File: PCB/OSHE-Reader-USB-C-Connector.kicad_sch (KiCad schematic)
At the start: 3 parts, among them J2 USB_C_Receptacle

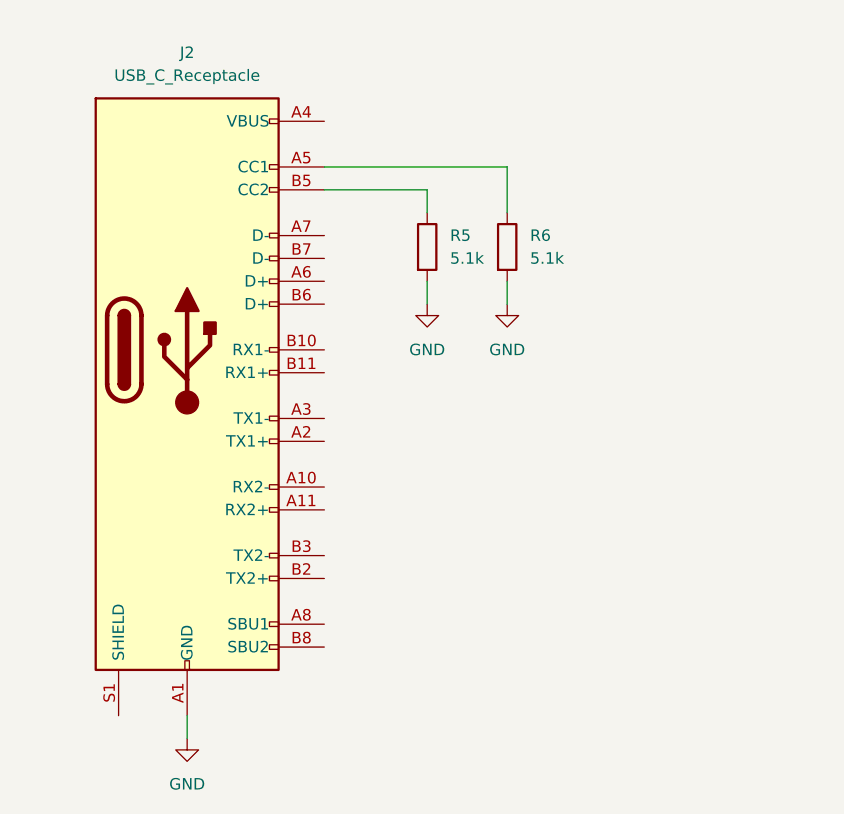
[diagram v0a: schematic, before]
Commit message: maybe finished usbc connector, depends on if we want to read CC lines for power adjustment
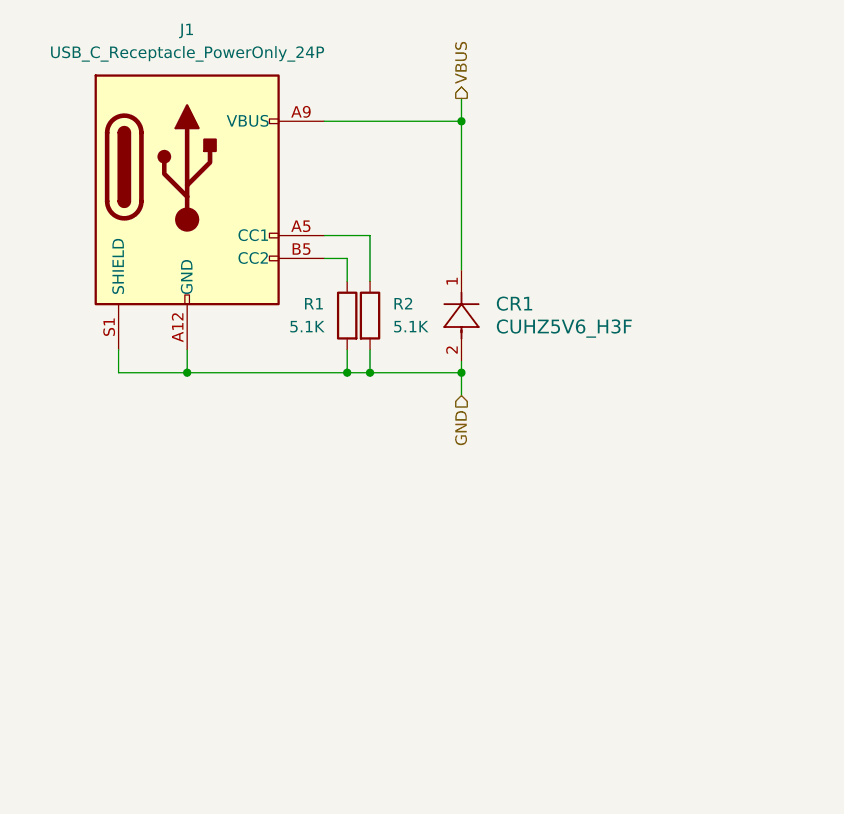
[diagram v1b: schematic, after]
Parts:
- removed J2: USB_C_Receptacle, symbol Connector:USB_C_Receptacle
- removed R5, R6: 5.1k, symbol Device:R
- added CR1: CUHZ5V6_H3F, SOD-323HEUS2H_TOS, symbol CUHZ5V6_H3F:CUHZ5V6_H3F
- added J1: USB_C_Receptacle_PowerOnly_24P, symbol Connector:USB_C_Receptacle_PowerOnly_24P
- added R1, R2: 5.1K, symbol Device:R
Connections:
- net GND: now also CR1.2, J1.A1 (GND), J1.A12 (GND), J1.B1 (GND), J1.B12 (GND), J1.S1 (SHIELD), R1.2, R2.2
- new net: J1.B5 (CC2), R1.1
- new net: J1.A5 (CC1), R2.1
- new net VBUS: CR1.1, J1.A4 (VBUS), J1.A9 (VBUS), J1.B4 (VBUS), J1.B9 (VBUS)

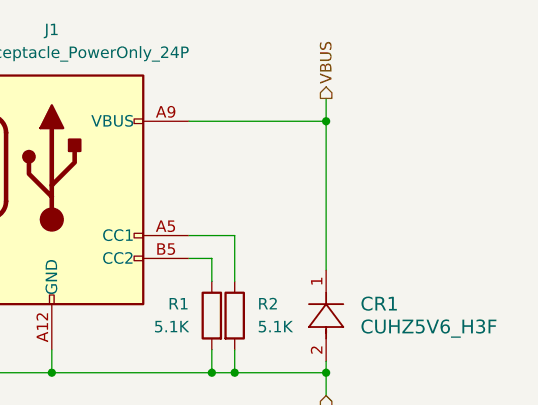
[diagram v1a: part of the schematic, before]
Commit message: fixed up the pcb so everything is *basically* passing ERC
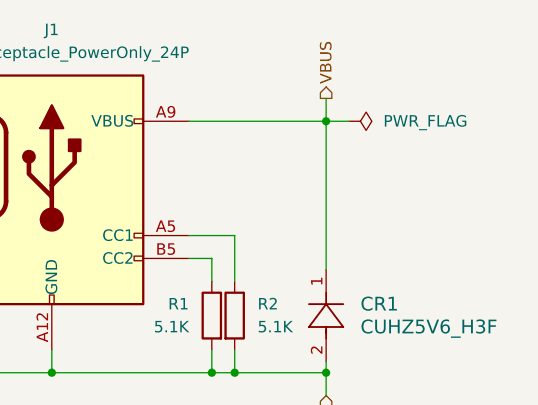
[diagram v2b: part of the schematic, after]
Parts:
- CR1: footprint SOD-323HEUS2H_TOS -> CUHZ5V6_H3F:SOD-323HEUS2H_TOS
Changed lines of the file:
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@@
+	(wire
+		(pts
+			(xy 68.58 33.02) (xy 71.12 33.02)
+		)
+		(stroke
+			(width 0)
+			(type default)
+		)
+	)
 	(wire
 		(pts
@@
 	)
 	(symbol
+		(lib_id "power:PWR_FLAG")
+		(at 71.12 33.02 270)
+		(unit 1)
+		(exclude_from_sim no)
+		(in_bom yes)
+		(on_board yes)
+		(dnp no)
+		(fields_autoplaced yes)
+		(property "Reference" "#FLG03"
+			(at 73.025 33.02 0)
+			(effects
+				(font
+					(size 1.27 1.27)
+				)
+				(hide yes)
+			)
+		)
+		(property "Value" "PWR_FLAG"
+			(at 74.93 33.0199 90)
+			(effects
+				(font
+					(size 1.27 1.27)
+				)
+				(justify left)
+			)
+		)
+		(property "Footprint" ""
+			(at 71.12 33.02 0)
+			(effects
+				(font
+					(size 1.27 1.27)
+				)
+				(hide yes)
+			)
+		)
+		(property "Datasheet" "~"
+			(at 71.12 33.02 0)
+			(effects
+				(font
+					(size 1.27 1.27)
+				)
+				(hide yes)
+			)
+		)
+		(property "Description" "Special symbol for telling ERC where power comes from"
+			(at 71.12 33.02 0)
+			(effects
+				(font
+					(size 1.27 1.27)
+				)
+				(hide yes)
+			)
+		)
+		(pin "1"
+		)
+		(instances
+			(project ""
+				(path "/3f072c92-e35a-4654-839b-728bd3dc3a46/026272d1-c63e-4075-9457-2aa47fc1f981"
+					(reference "#FLG03")
+					(unit 1)
+				)
+			)
+		)
+	)
+	(symbol
 		(lib_id "CUHZ5V6_H3F:CUHZ5V6_H3F")
 		(at 68.58 59.69 90)
@@
 			)
 		)
-		(property "Footprint" "SOD-323HEUS2H_TOS"
+		(property "Footprint" "CUHZ5V6_H3F:SOD-323HEUS2H_TOS"
 			(at 68.58 59.69 0)
 			(effects

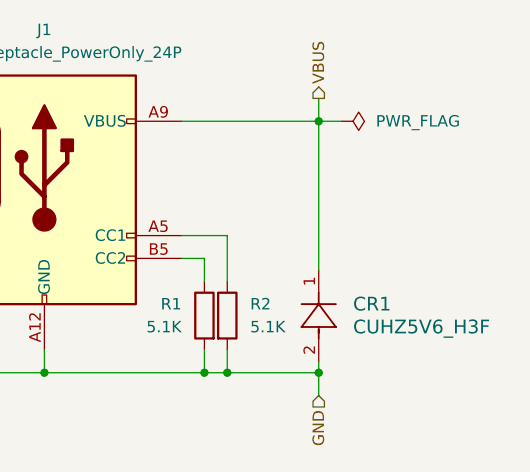
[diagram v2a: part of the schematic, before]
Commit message: work on pcb, adjusted components and started building ribbon connector for display
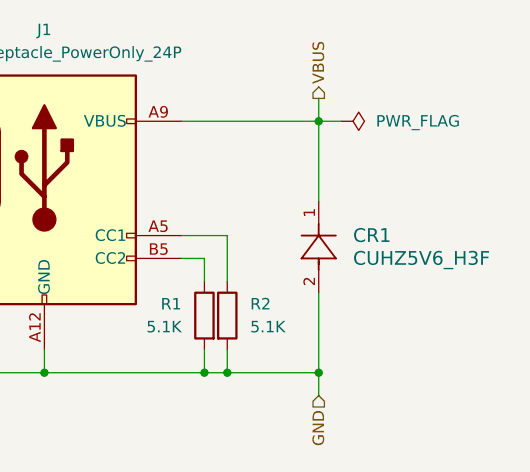
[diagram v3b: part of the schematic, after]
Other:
- moved on the sheet: CR1
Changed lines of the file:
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@@
 	(wire
 		(pts
-			(xy 68.58 60.96) (xy 68.58 59.69)
-		)
-		(stroke
-			(width 0)
-			(type default)
-		)
-	)
-	(wire
-		(pts
-			(xy 68.58 49.53) (xy 68.58 33.02)
+			(xy 68.58 60.96) (xy 68.58 52.07)
+		)
+		(stroke
+			(width 0)
+			(type default)
+		)
+	)
+	(wire
+		(pts
+			(xy 68.58 41.91) (xy 68.58 33.02)
 		)
 		(stroke
@@
 	(symbol
 		(lib_id "CUHZ5V6_H3F:CUHZ5V6_H3F")
-		(at 68.58 59.69 90)
+		(at 68.58 52.07 90)
 		(unit 1)
 		(exclude_from_sim no)
@@
 		(fields_autoplaced yes)
 		(property "Reference" "CR1"
-			(at 72.39 53.3399 90)
+			(at 72.39 45.7199 90)
 			(effects
 				(font
@@
 		)
 		(property "Value" "CUHZ5V6_H3F"
-			(at 72.39 55.8799 90)
+			(at 72.39 48.2599 90)
 			(effects
 				(font
@@
 		)
 		(property "Footprint" "CUHZ5V6_H3F:SOD-323HEUS2H_TOS"
-			(at 68.58 59.69 0)
+			(at 68.58 52.07 0)
 			(effects
 				(font
@@
 		)
 		(property "Datasheet" "https://toshiba.semicon-storage.com/info/docget.jsp?did=141580&prodName=CUHZ5V6"
-			(at 68.58 59.69 0)
+			(at 68.58 52.07 0)
 			(effects
 				(font
@@
 		)
 		(property "Description" ""
-			(at 68.58 59.69 0)
-			(effects
-				(font
+			(at 68.58 52.07 0)
+			(effects
+				(font

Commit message: added usbc connector symbol, footprint, and model, updated symbol in schematic
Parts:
- J1: footprint (none) -> USB4125_GF_A:CONN6_USB4125_GCT
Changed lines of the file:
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@@
 			)
 		)
-		(property "Footprint" ""
+		(property "Footprint" "USB4125_GF_A:CONN6_USB4125_GCT"
 			(at 41.91 38.1 0)
 			(effects

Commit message: HOPEFULLY GOOD FOR EVER (good for first semester) :)
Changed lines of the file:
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@@
-	(wire
-		(pts
-			(xy 68.58 33.02) (xy 71.12 33.02)
-		)
-		(stroke
-			(width 0)
-			(type default)
-		)
-	)
 	(wire
 		(pts
@@
 	)
 	(hierarchical_label "GND"
-		(shape input)
+		(shape output)
 		(at 68.58 63.5 270)
 		(effects
@@
 					(unit 1)
 				)
-			)
-		)
-	)
-	(symbol
-		(lib_id "power:PWR_FLAG")
-		(at 71.12 33.02 270)
-		(unit 1)
-		(exclude_from_sim no)
-		(in_bom yes)
-		(on_board yes)
-		(dnp no)
-		(fields_autoplaced yes)
-		(property "Reference" "#FLG03"
-			(at 73.025 33.02 0)
-			(effects
-				(font
-					(size 1.27 1.27)
-				)
-				(hide yes)
-			)
-		)
-		(property "Value" "PWR_FLAG"
-			(at 74.93 33.0199 90)
-			(effects
-				(font
-					(size 1.27 1.27)
-				)
-				(justify left)
-			)
-		)
-		(property "Footprint" ""
-			(at 71.12 33.02 0)
-			(effects
-				(font
-					(size 1.27 1.27)
-				)
-				(hide yes)
-			)
-		)
-		(property "Datasheet" "~"
-			(at 71.12 33.02 0)
-			(effects
-				(font
-					(size 1.27 1.27)
-				)
-				(hide yes)
-			)
-		)
-		(property "Description" "Special symbol for telling ERC where power comes from"
-			(at 71.12 33.02 0)
-			(effects
-				(font
-					(size 1.27 1.27)
-				)
-				(hide yes)
-			)
-		)
-		(pin "1"
-		)
-		(instances
-			(project ""
-				(path "/3f072c92-e35a-4654-839b-728bd3dc3a46/026272d1-c63e-4075-9457-2aa47fc1f981"
-					(reference "#FLG03")
-					(unit 1)
-				)

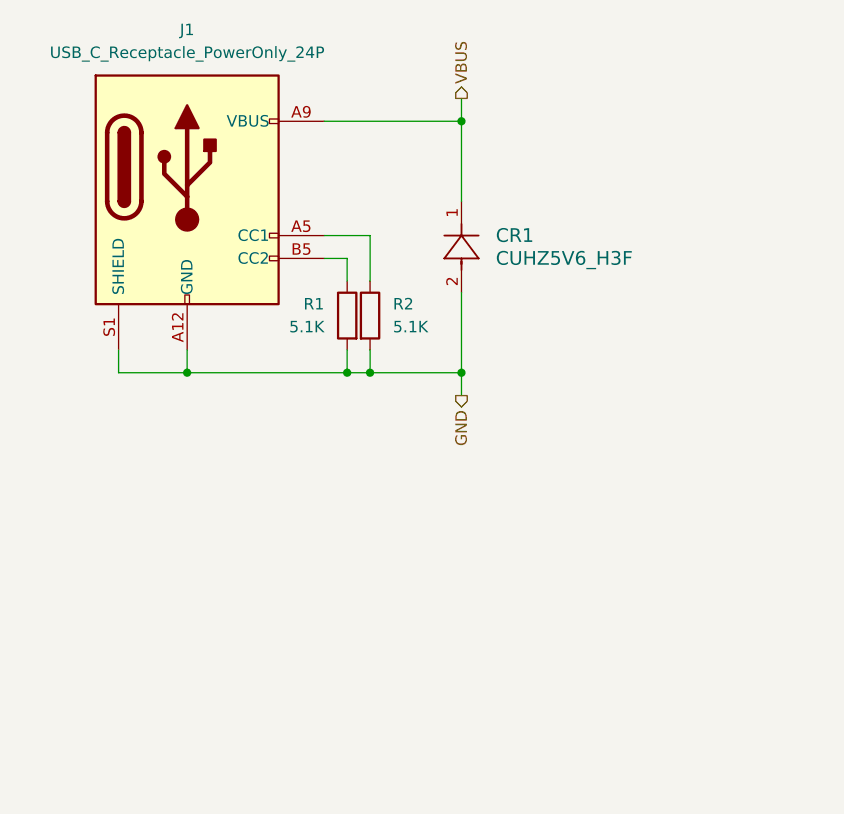
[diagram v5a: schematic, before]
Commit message: Footprints added
All footprints added (problem with J1 for some reason) ((pads of the display driver))
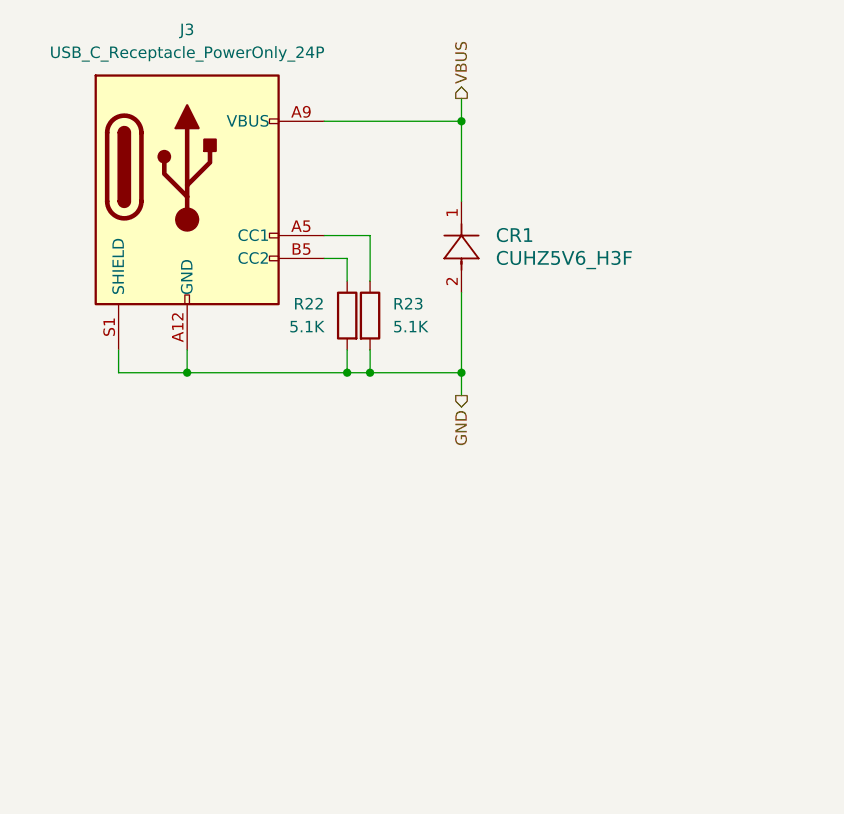
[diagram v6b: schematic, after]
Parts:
- R22: renamed from R1; footprint (none) -> Resistor_SMD:R_1206_3216Metric
- R23: renamed from R2; footprint (none) -> Resistor_SMD:R_1206_3216Metric
- renumbered J1 to J3
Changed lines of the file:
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@@
 		(on_board yes)
 		(dnp no)
-		(property "Reference" "R1"
+		(property "Reference" "R22"
 			(at 53.34 53.3399 0)
 			(effects
@@
 			)
 		)
-		(property "Footprint" ""
+		(property "Footprint" "Resistor_SMD:R_1206_3216Metric"
 			(at 57.658 54.61 90)
 			(effects
@@
 		)
 		(instances
+			(project "OSHE-Reader-USB-C-Connector"
+				(path "/2ea26629-c50f-40b4-9df1-27f728ca0091"
+					(reference "R22")
+					(unit 1)
+				)
+			)
 			(project ""
 				(path "/3f072c92-e35a-4654-839b-728bd3dc3a46/026272d1-c63e-4075-9457-2aa47fc1f981"
@@
 		(dnp no)
 		(fields_autoplaced yes)
-		(property "Reference" "J1"
+		(property "Reference" "J3"
 			(at 38.1 22.86 0)
 			(effects
@@
 		)
 		(instances
+			(project "OSHE-Reader-USB-C-Connector"
+				(path "/2ea26629-c50f-40b4-9df1-27f728ca0091"
+					(reference "J3")
+					(unit 1)
+				)
+			)
 			(project ""
 				(path "/3f072c92-e35a-4654-839b-728bd3dc3a46/026272d1-c63e-4075-9457-2aa47fc1f981"
@@
 		)
 		(instances
+			(project "OSHE-Reader-USB-C-Connector"
+				(path "/2ea26629-c50f-40b4-9df1-27f728ca0091"
+					(reference "CR1")
+					(unit 1)
+				)
+			)
 			(project ""
 				(path "/3f072c92-e35a-4654-839b-728bd3dc3a46/026272d1-c63e-4075-9457-2aa47fc1f981"
@@
 		(dnp no)
 		(fields_autoplaced yes)
-		(property "Reference" "R2"
+		(property "Reference" "R23"
 			(at 60.96 53.3399 0)
 			(effects
@@
 			)
 		)
-		(property "Footprint" ""
+		(property "Footprint" "Resistor_SMD:R_1206_3216Metric"
 			(at 56.642 54.61 90)
 			(effects
@@
 		)
 		(instances
+			(project "OSHE-Reader-USB-C-Connector"
+				(path "/2ea26629-c50f-40b4-9df1-27f728ca0091"
+					(reference "R23")
+					(unit 1)
+				)
+			)
 			(project "OSHE-Reader-PCB"
 				(path "/3f072c92-e35a-4654-839b-728bd3dc3a46/026272d1-c63e-4075-9457-2aa47fc1f981"
@@
 		)
 	)
+	(sheet_instances
+		(path "/"
+			(page "1")
+		)
+	)
+	(embedded_fonts no)
 )

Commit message: Did a bunch of work with final preparations of the schematic for pcb routing
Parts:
- removed J3: USB_C_Receptacle_PowerOnly_24P, USB4125_GF_A:CONN6_USB4125_GCT, symbol Connector:USB_C_Receptacle_PowerOnly_24P
- removed R22, R23: 5.1K, Resistor_SMD:R_1206_3216Metric, symbol Device:R
- added J1: 2171750001, 2171750001_MOL, symbol 2171750001:2171750001
- added R1, R2: 5.1k, Resistor_SMD:R_1206_3216Metric, symbol Device:R
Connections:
- net GND: now also J1.A12 (GND), J1.B12 (GND), R1.1, R2.2
- net VBUS: now also J1.A9 (VBUS), J1.B9 (VBUS)
- new net: J1.A5 (CC1), R1.2
- new net: J1.B5 (CC2), R2.1
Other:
- moved on the sheet: CR1
